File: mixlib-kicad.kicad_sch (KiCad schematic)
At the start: 12 parts, among them Q2 AO3401A, U1 MCP6401, U2 MCP6401

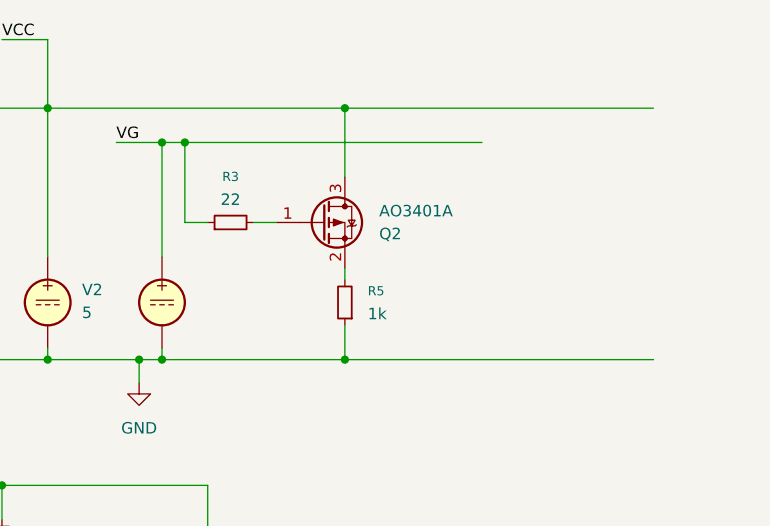
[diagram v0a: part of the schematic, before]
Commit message: fix: simplify some MOSFET footprints and add missing simulation scripts
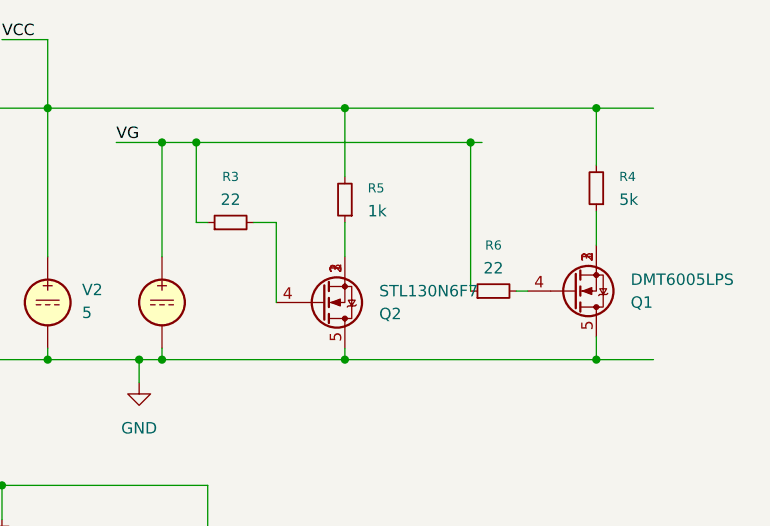
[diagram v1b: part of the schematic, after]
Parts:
- removed Q2: AO3401A, Package_TO_SOT_SMD:SOT-23, symbol mixlib-discrete-mosfet:AO3401A
- added Q1: DMT6005LPS, mixlib-discrete-mosfet:POWERDI5060-8, symbol mixlib-discrete-mosfet:DMT6005LPS
- added Q2: STL130N6F7, mixlib-discrete-mosfet:POWERFLAT_5X6_C_STM, symbol mixlib-discrete-mosfet:STL130N6F7
- added R4: 5k, symbol Device:R_Small
- added R6: 22, symbol Device:R_Small
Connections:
- net GND: now also Q1.5 (D), Q2.5 (D); no longer R5.1
- net VCC: now also R5.2, R4.2
- net VG: now also R6.1
- net at R3.2: now also Q2.4 (G)
- new net: Q1.1 (S), Q1.2 (S), Q1.3 (S), R4.1
- new net: Q1.4 (G), R6.2
- new net: Q2.1 (S), Q2.2 (S), Q2.3 (S), R5.1
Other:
- moved on the sheet: R5

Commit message: chore: saving project state
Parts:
- removed Q1: DMT6005LPS, mixlib-discrete-mosfet:POWERDI5060-8, symbol mixlib-discrete-mosfet:DMT6005LPS
- removed Q2: STL130N6F7, mixlib-discrete-mosfet:POWERFLAT_5X6_C_STM, symbol mixlib-discrete-mosfet:STL130N6F7
- removed R4: 5k, symbol Device:R_Small
- removed R5: 1k, symbol Device:R_Small
- removed R6: 22, symbol Device:R_Small
- added Q1, Q2: MMBT5551L, Package_TO_SOT_SMD:SOT-23, symbol mixlib-discrete-npn:MMBT5551L
- R3: value 22 -> 10k
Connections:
- net GND: now also Q2.2 (E); no longer R1.1, R2.1
- net VCC: now also R2.2
- net VG: no longer R3.1
- net at R3.2: now also U1.1
- removed net VOUT1: R2.2, U1.1
- net VOUT2: no longer names the net of R1.2, U2.1
- new net: Q1.1 (B), R3.1
- new net: Q1.3 (C), R2.1
- new net: Q2.1 (B), R1.1
- new net: Q1.2 (E), Q2.3 (C)
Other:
- moved on the sheet: R1

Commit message: fix: various fixes
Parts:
- added D1: BZT52C3V3, Diode_SMD:D_SOD-123, symbol mixlib-discrete-zener:BZT52Cxx
- added R4: 10k, symbol Device:R_Small
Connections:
- net GND: now also R4.1
- net VG: now also D1.1 (K)
- new net VOUT: D1.2 (A), R4.2

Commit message: feat: add some bjt transistors and fix simulation scripts
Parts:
- removed D1: BZT52C3V3, Diode_SMD:D_SOD-123, symbol mixlib-discrete-zener:BZT52Cxx
- removed U1, U2: MCP6401, Package_TO_SOT_SMD:SOT-353_SC-70-5, symbol mixlib-analog-opamp:MCP6401
- added R10: 560, symbol Device:R_Small
- added R16, R18, R19, R20, R21, R5, R6, R7, R8: 10k, symbol Device:R_Small
- added R17, R22: 200k, symbol Device:R_Small
- added R9: 1.5k, symbol Device:R_Small
- added U1: ADA4522-4, symbol mixlib-analog-opamp:ADA4522-4
- added U2: MCP6404, Package_SO:SOIC-14_3.9x8.7mm_P1.27mm, symbol mixlib-analog-opamp:MCP6404
- added U3: ADA4522-2, symbol mixlib-analog-opamp:ADA4522-2
- added V3: VSIN, symbol Simulation_SPICE:VSIN
- added V4: 2.5, symbol Simulation_SPICE:VDC
- added V5: 45, symbol Simulation_SPICE:VDC
- V1: value 30 -> 50
- V2: value 5 -> 50
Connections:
- net GND: now also Q1.2 (E), R8.1, U1.11 (V-), U2.11 (V-), U3.4 (V-), V3.2, V4.2, V5.2; no longer R4.1
- net VCC: now also R7.2, U1.4 (V+), U2.4 (V+), U3.8 (V+)
- net VG: now also U3.2 (-), U3.5 (+)
- net VOUT: now also Q1.3 (C), Q2.3 (C), R2.1; no longer R4.2
- net VOUT_TOP: now reaches R3.2
- net VOUT_TOP: now also U3.1
- net VREF_BOT: now reaches R12.1, R13.2
- net VREF_BOT: now also U3.6 (-)
- net VREF_TOP: now reaches R11.1, R12.2
- net VREF_TOP: now also U3.3 (+)
- net VOUT_BOT: now reaches R1.2
- net VOUT_BOT: now also U3.7
- new net: R16.1, R19.2, U1.9 (-)
- new net: R21.1, R22.2, U1.12 (+)
- new net: R10.1, R5.2, R9.1, U1.6 (-)
- new net: R10.2, R6.1, R9.2, U1.2 (-)
- new net: R18.1, R4.2, U1.10 (+)
- new net: R17.2, R20.1, U1.13 (-)
- new net VMID: R7.1, R8.2
- new net VREF: R22.1, R4.1, V4.1
- new net VSIN_CMP_BOT: R18.2, R5.1, U1.7
- new net VSIN_CMP_TOP: R16.2, R6.2, U1.1
- new net VSIN_IN: R21.2, U1.5 (+), V3.1
- new net VSIN_OUT: R19.1, U1.8
- new net VSIN_OUT2: R17.1, U1.14
- new net VSIN_VREF: R20.2, U1.3 (+), V5.1
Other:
- moved on the sheet: Q1, Q2, R1, R11, R12, R13, R2, R3, V2

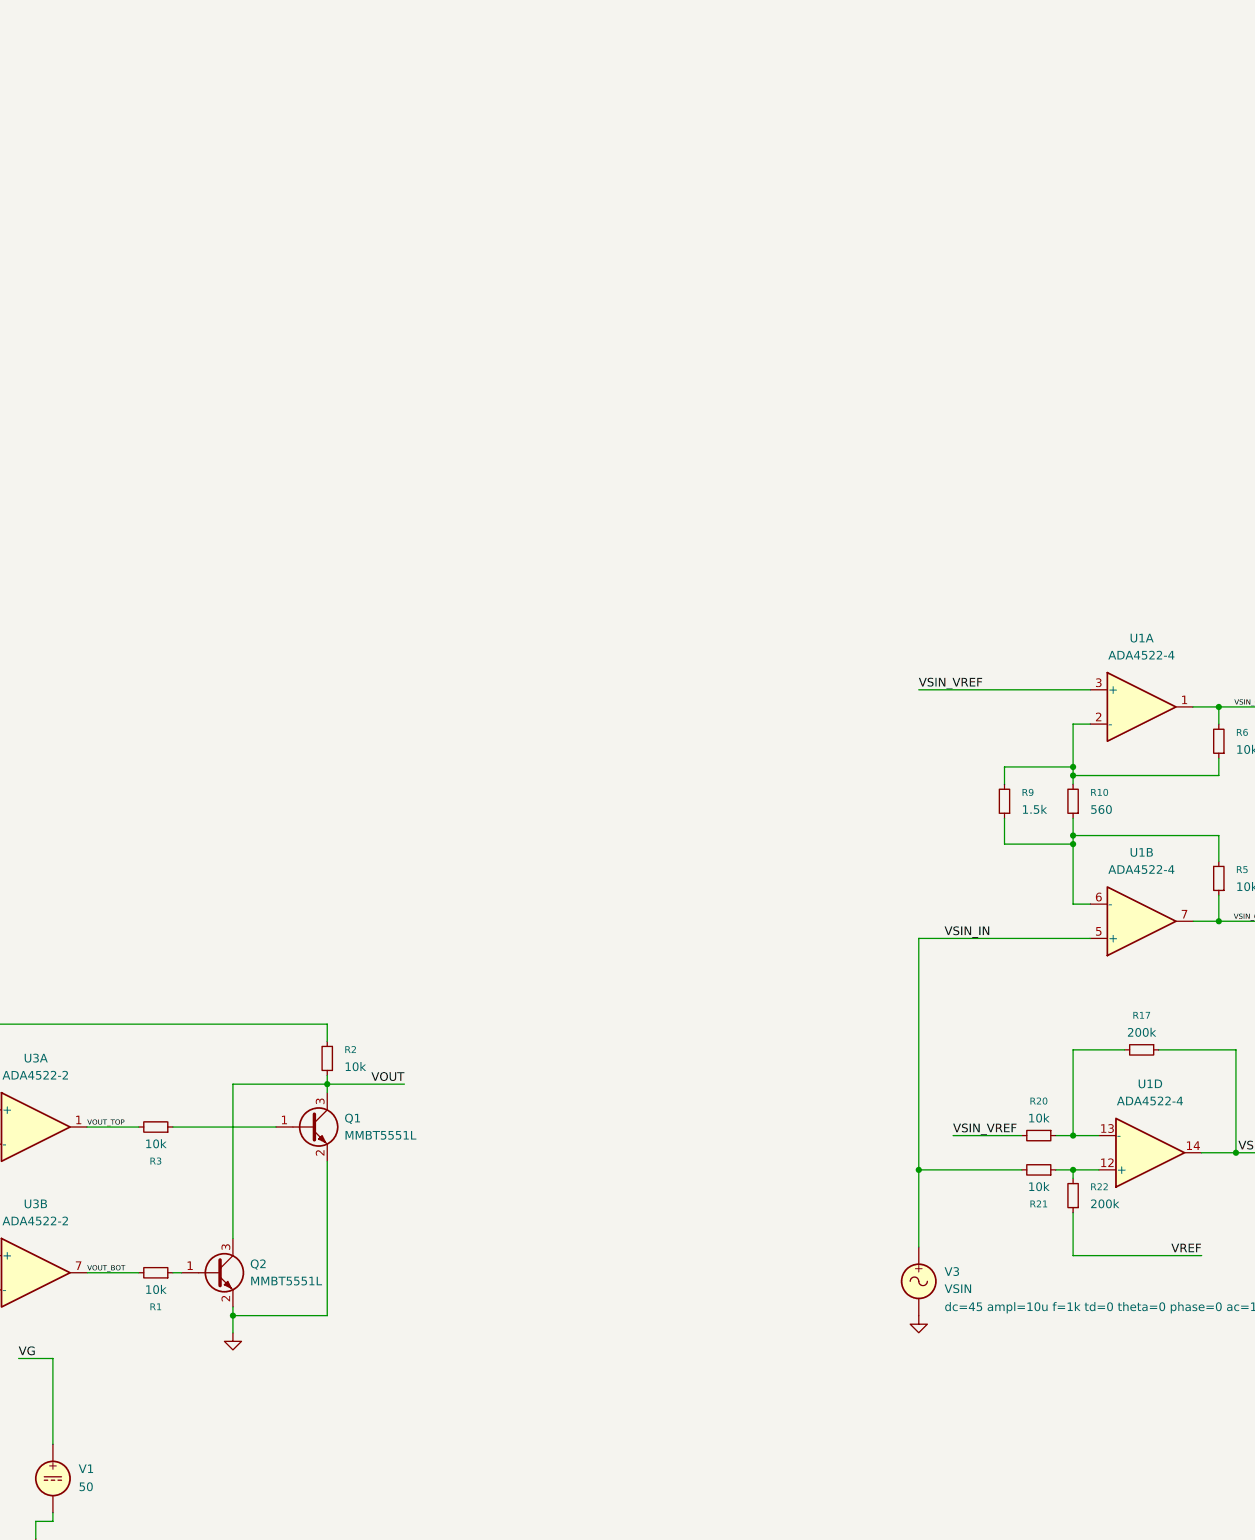
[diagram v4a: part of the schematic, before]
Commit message: feat: add some bjt transistors and fix simulation scripts
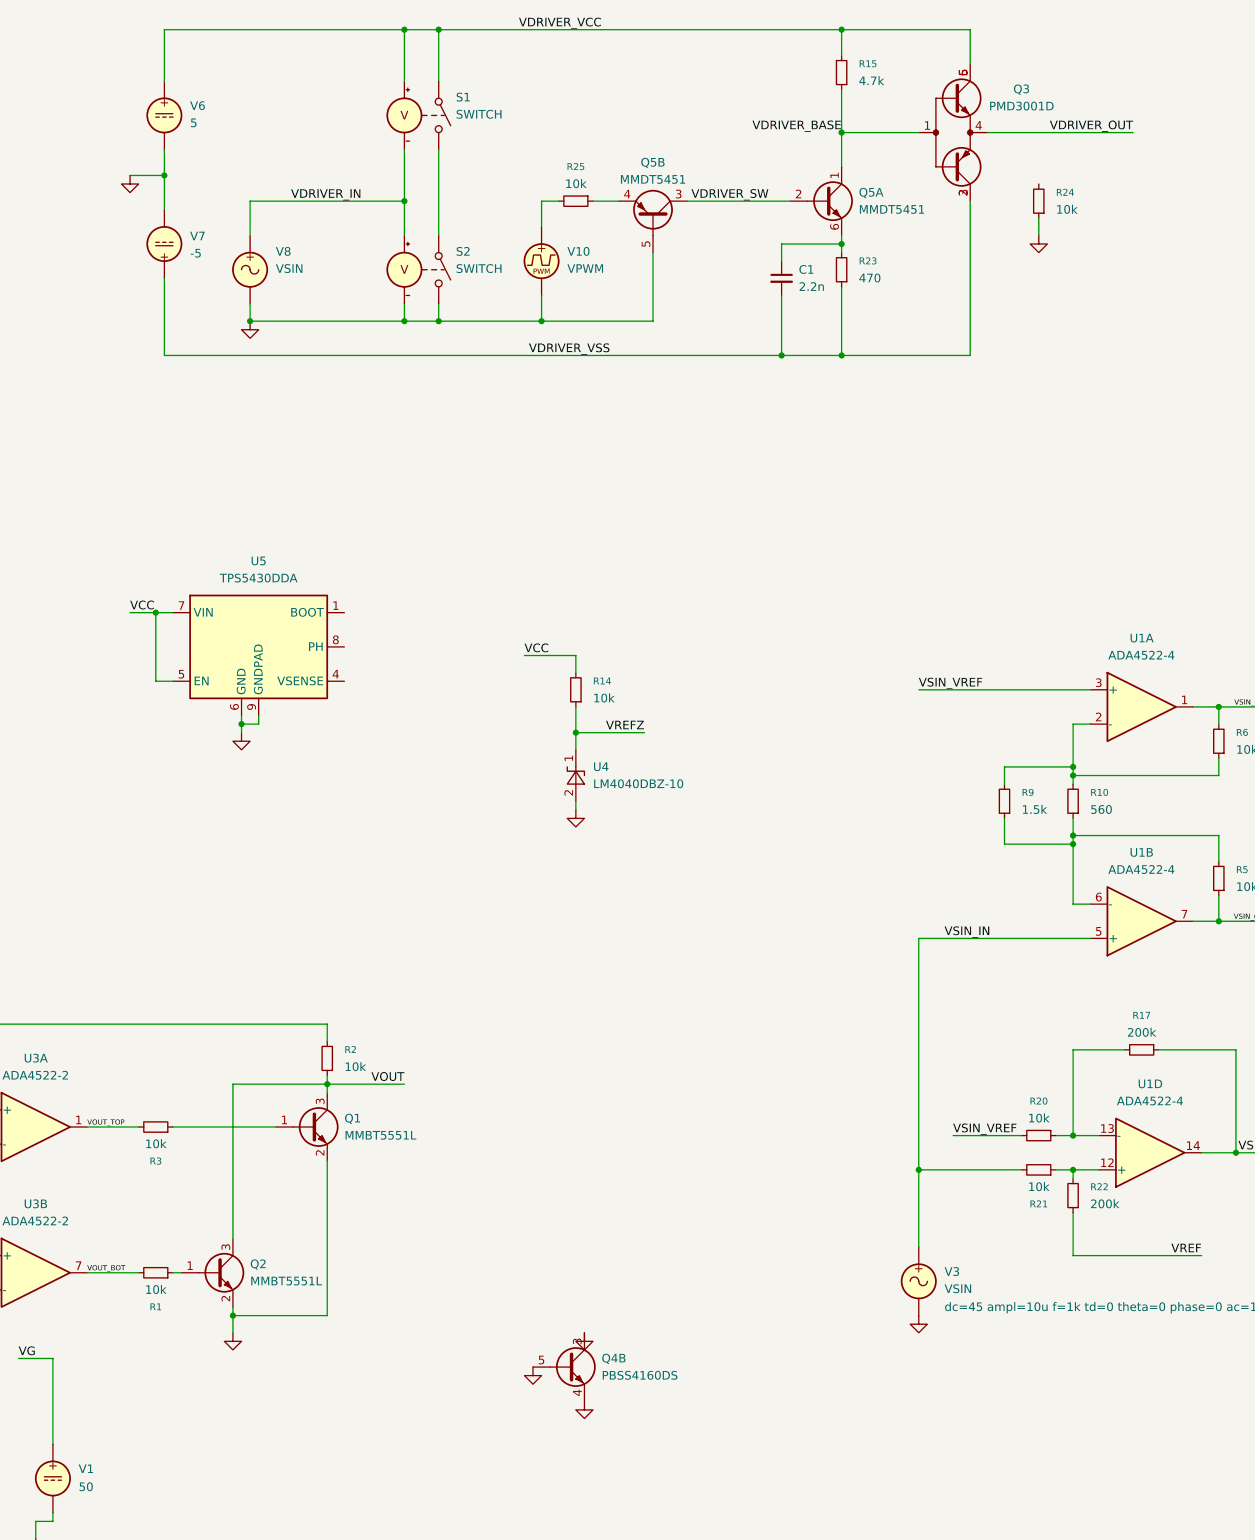
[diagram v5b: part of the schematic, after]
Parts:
- added C1: 2.2n, symbol Device:C_Small
- added Q3: PMD3001D, mixlib-generic-sot:SC-74_SOT-457_NEX, symbol mixlib-discrete-npnpnp:PMD3001D
- added Q4: PBSS4160DS, mixlib-generic-sot:SC-74_SOT-457_NEX, symbol mixlib-discrete-npn:PBSS4160DS
- added Q5: MMDT5451, mixlib-generic-sot:SOT-363_SC-70-6, symbol mixlib-discrete-npnpnp:MMDT5451
- added R14, R24, R25: 10k, symbol Device:R_Small
- added R15: 4.7k, symbol Device:R_Small
- added R23: 470, symbol Device:R_Small
- added S1, S2: SWITCH, symbol Simulation_SPICE:SWITCH
- added U4: LM4040DBZ-10, Package_TO_SOT_SMD:SOT-23, symbol Reference_Voltage:LM4040DBZ-10
- added U5: TPS5430DDA, Package_SO:TI_SO-PowerPAD-8_ThermalVias, symbol mixlib-pmic-vreg:TPS5430DDA
- added V10: VPWM, symbol mixlib-sim-vsource:VPWM
- added V6: 5, symbol Simulation_SPICE:VDC
- added V7: -5, symbol Simulation_SPICE:VDC
- added V8: VSIN, symbol Simulation_SPICE:VSIN
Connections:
- net GND: now also Q4.3 (C2), Q4.4 (E2), Q4.5 (B2), Q5.5 (B2), R24.1, S2.2 (N-), S2.4 (C-), U4.2 (A), U5.6 (GND), U5.9 (GNDPAD), V10.2, V6.2, V7.2, V8.2
- net VCC: now also R14.2, U5.5 (EN), U5.7 (VIN)
- new net: C1.1, Q5.6 (E1), R23.2
- new net: S1.2 (N-), S2.1 (N+)
- new net: R25.2, V10.1
- new net: Q5.4 (E2), R25.1
- new net VDRIVER_BASE: Q3.1 (B), Q5.1 (C1), R15.1
- new net VDRIVER_IN: S1.4 (C-), S2.3 (C+), V8.1
- new net VDRIVER_OUT: Q3.4 (E)
- new net VDRIVER_SW: Q5.2 (B1), Q5.3 (C2)
- new net VDRIVER_VCC: Q3.5 (C1_1), Q3.6 (C1_2), R15.2, S1.1 (N+), S1.3 (C+), V6.1
- new net VDRIVER_VSS: C1.2, Q3.2 (C2_1), Q3.3 (C2_2), R23.1, V7.1
- new net VREFZ: R14.1, U4.1 (K)

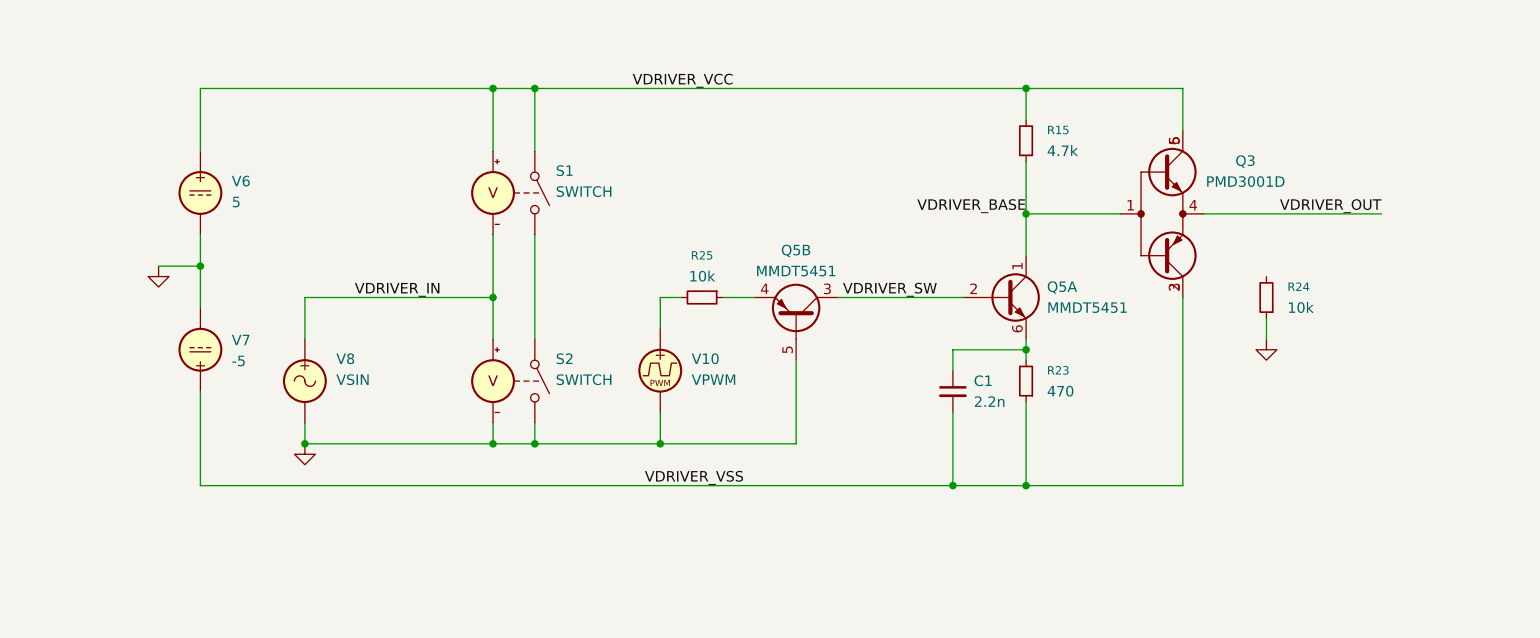
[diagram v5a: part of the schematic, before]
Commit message: feat(discrete/npn): PMD3001D: redesign symbol
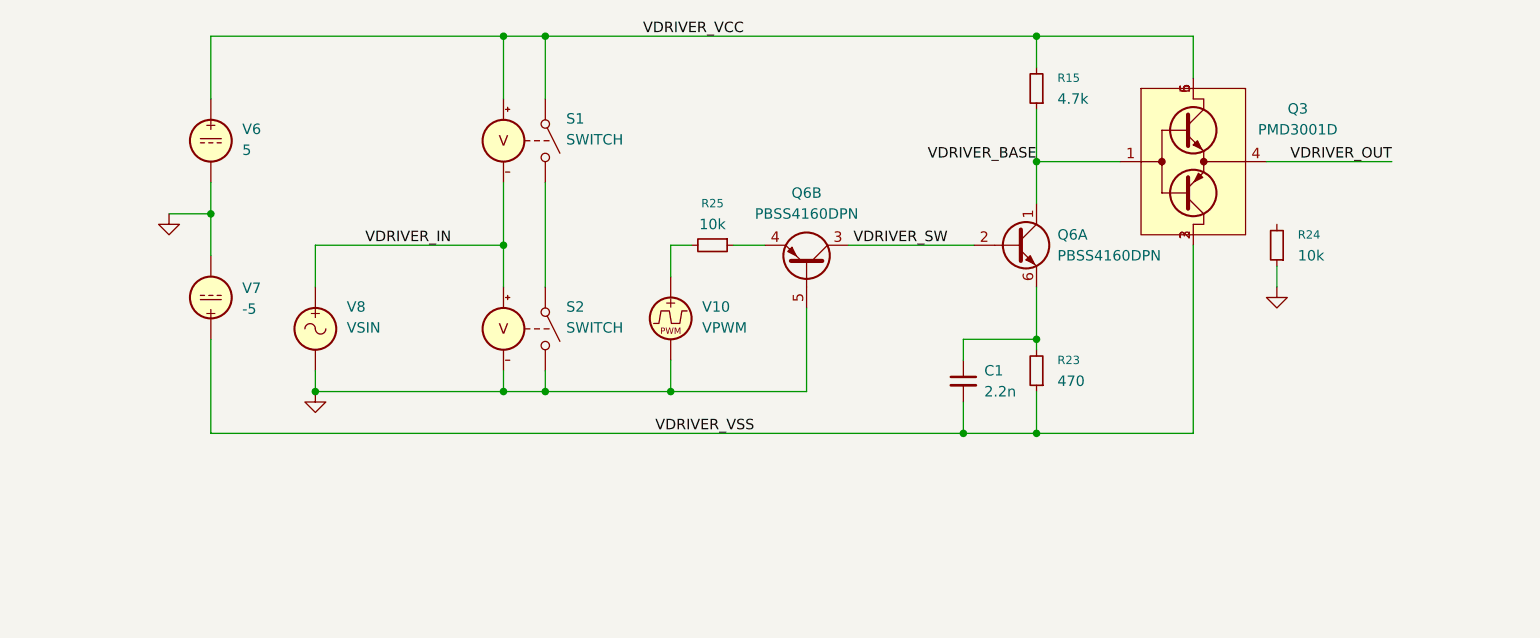
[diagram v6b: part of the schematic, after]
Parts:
- removed Q5: MMDT5451, mixlib-generic-sot:SOT-363_SC-70-6, symbol mixlib-discrete-npnpnp:MMDT5451
- added Q6: PBSS4160DPN, mixlib-generic-sot:SC-74_SOT-457_NEX, symbol mixlib-discrete-npnpnp:PBSS4160DPN
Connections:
- net GND: now also Q6.5 (B2)
- net VDRIVER_BASE: now also Q6.1 (C1)
- net VDRIVER_SW: now also Q6.2 (B1), Q6.3 (C2)
- net at C1.1, R23.2: now also Q6.6 (E1)
- net at R25.1: now also Q6.4 (E2)
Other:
- moved on the sheet: C1, R15, R23, R24, R25, S1, S2, V10, V6, V7, V8
